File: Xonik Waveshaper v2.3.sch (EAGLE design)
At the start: 77 parts, among them IC1 TL074JT, IC2 TL074JT, IC3 TL074JT, IC4 TL072JT, IC5 4013T, IC6 LM311D, T1 2n3904

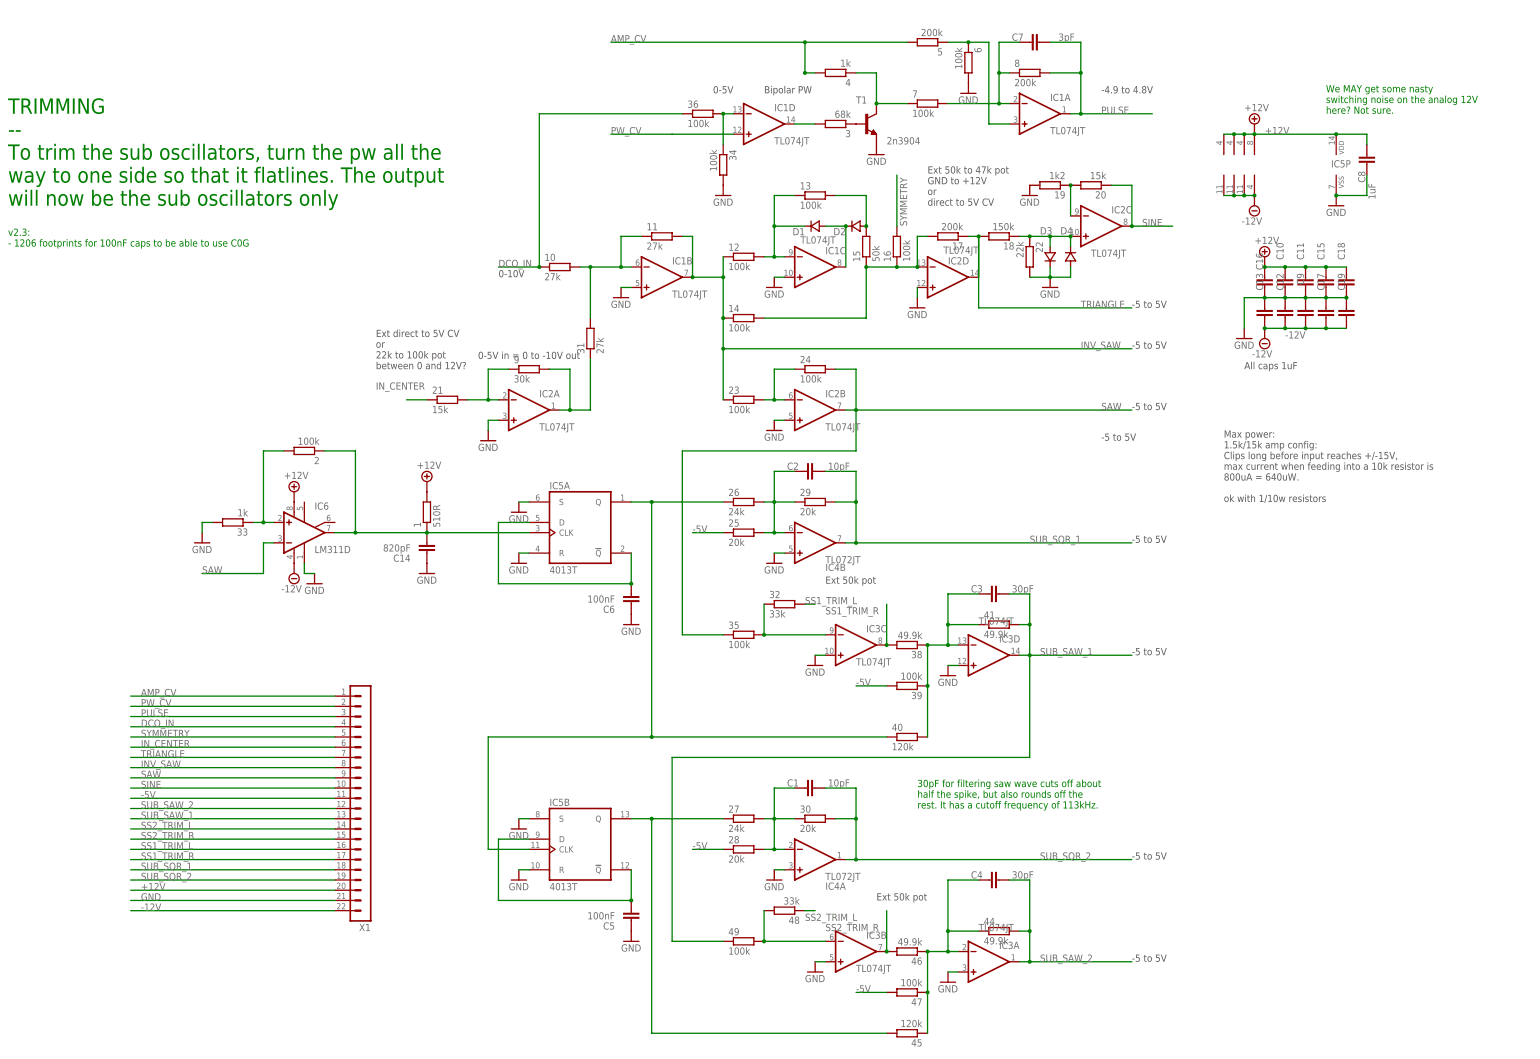
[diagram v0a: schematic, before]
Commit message: Replaced LM311 with op amp comparator
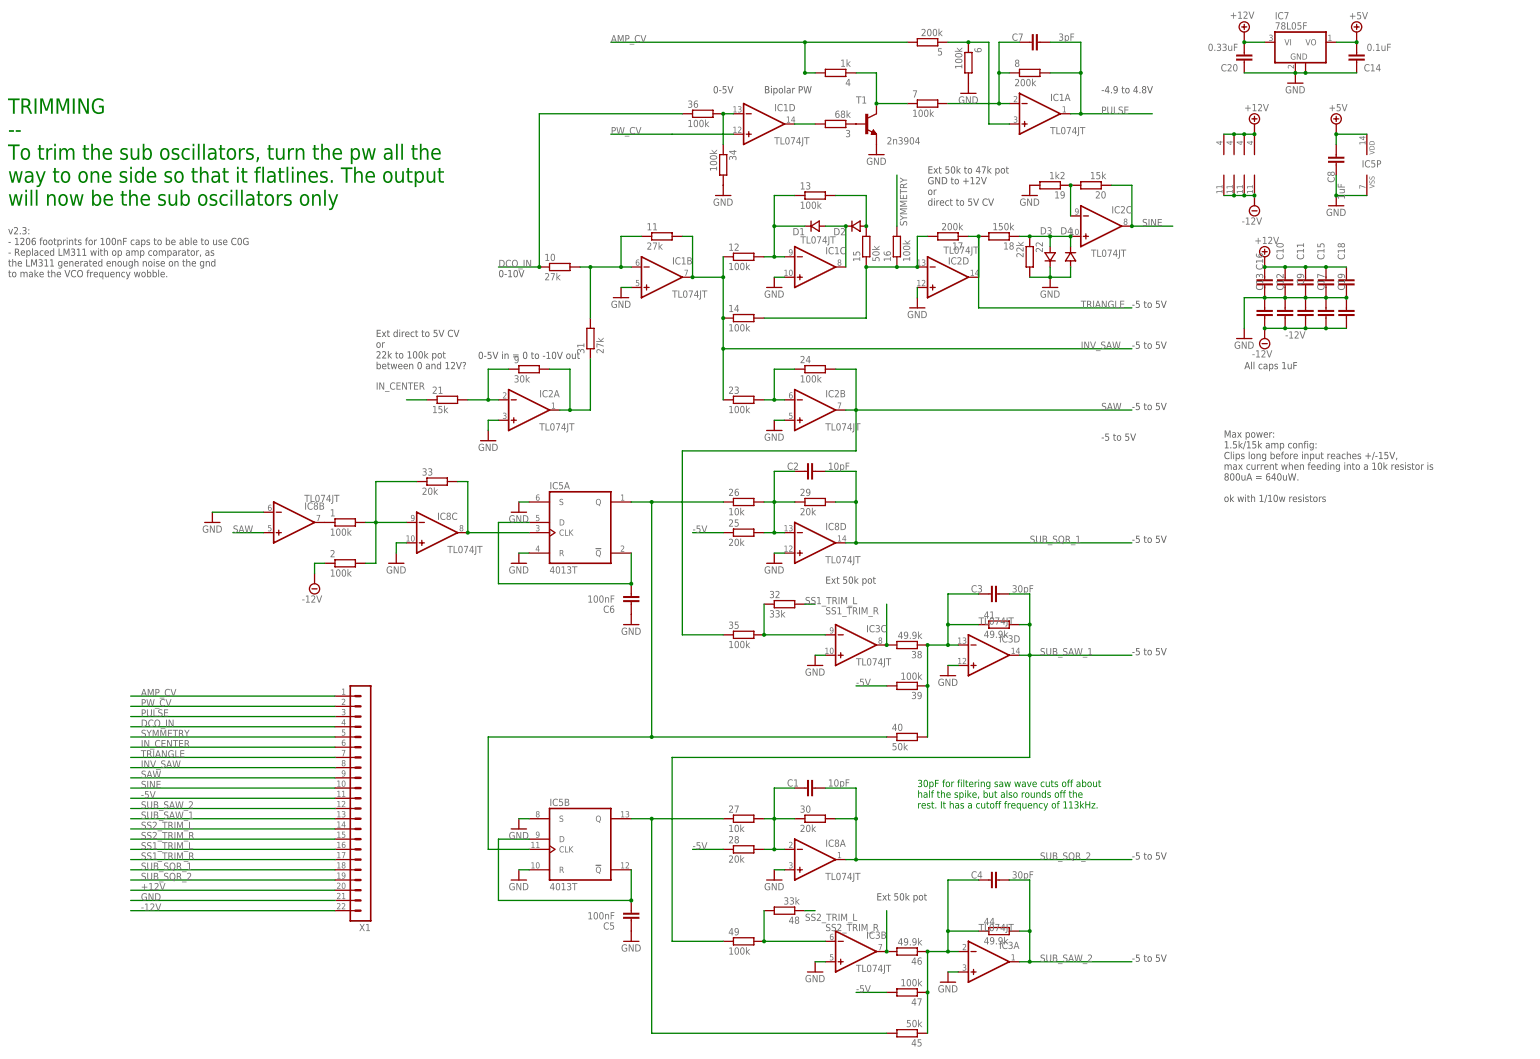
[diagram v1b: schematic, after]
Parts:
- removed IC4: TL072JT, joakim:TL072JT
- removed IC6: LM311D, joakim:LM311D
- added C20: 0.33uF, resistor:C-EUC0603
- added IC7: 78L05F, linear:78L05F
- added IC8: TL074JT, joakim:TL074JT
- 1: value 510R -> 100k
- 26, 27: value 24k -> 10k
- 33: value 1k -> 20k
- 40, 45: value 120k -> 50k
- C14: value 820pF -> 0.1uF; device joakim:C-EU-J0603 -> resistor:C-EUC0603
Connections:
- removed net N$25: 2.2, 33.1, IC6.+IN
- removed net SQR: 1.1, 2.1, C14.2, IC5A.CLK, IC6.OUT
- new net +5V: C14.2, C8.2, IC5P.VDD, IC7.VO
- new net N$17: 33.2, IC5A.CLK, IC8C.OUT
- new net N$7: 1.1, IC8B.OUT
- new net N$9: 1.2, 2.2, 33.1, IC8C.-IN
- net +12V: now also C20.2, IC7.VI, IC8P.V+; no longer 1.2, C8.2, IC4P.V+, IC5P.VDD, IC6.V+
- net -12V: now also 2.1, IC8P.V-; no longer IC4P.V-, IC6.V-
- net GND: now also C20.1, IC7.GND, IC7.GND@1, IC8A.+IN, IC8B.-IN, IC8C.+IN, IC8D.+IN; no longer 33.2, IC4A.+IN, IC4B.+IN, IC6.GND
- net N$19: now also IC8D.-IN; no longer IC4B.-IN
- net N$22: now also IC8A.-IN; no longer IC4A.-IN
- net SAW: now also IC8B.+IN; no longer IC6.-IN
- net SUB_SQR_1: now also IC8D.OUT; no longer IC4B.OUT
- net SUB_SQR_2: now also IC8A.OUT; no longer IC4A.OUT
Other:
- note added: "v2.3: - 1206 footprints for 100nF caps to be able to use C0G - Replaced LM311 with op amp comparator, as the LM311 generated enough noise on the gnd to make the VCO frequency wobble."
- note removed: "We MAY get some nasty switching noise on the analog 12V here? Not sure."
- note removed: "v2.3: - 1206 footprints for 100nF caps to be able to use C0G"
- moved on the sheet: 1, 2, 33, C14, C8, IC5P

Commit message: Routed new version of comparator
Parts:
- removed C14: 0.1uF, resistor:C-EUC0603
- removed C18, C19: 1uF, joakim:C-EU-J0402
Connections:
- net +12V: no longer C18.2
- net +5V: no longer C14.2
- net -12V: no longer C19.1
- net GND: no longer C14.1, C18.1, C19.2
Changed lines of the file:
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@@
 <part name="C15" library="joakim" deviceset="C-EU-J" device="0402" value="1uF"/>
 <part name="C17" library="joakim" deviceset="C-EU-J" device="0402" value="1uF"/>
-<part name="C18" library="joakim" deviceset="C-EU-J" device="0402" value="1uF"/>
-<part name="C19" library="joakim" deviceset="C-EU-J" device="0402" value="1uF"/>
 <part name="34" library="rcl" library_urn="urn:adsk.eagle:library:334" deviceset="R-EU_" device="R0402" package3d_urn="urn:adsk.eagle:package:23547/3" value="100k"/>
 <part name="36" library="rcl" library_urn="urn:adsk.eagle:library:334" deviceset="R-EU_" device="R0402" package3d_urn="urn:adsk.eagle:package:23547/3" value="100k"/>
@@
 <part name="IC7" library="linear" library_urn="urn:adsk.eagle:library:262" deviceset="78L*" device="F" package3d_urn="urn:adsk.eagle:package:16478/2" technology="05"/>
 <part name="SUPPLY5" library="supply2" library_urn="urn:adsk.eagle:library:372" deviceset="+5V" device=""/>
-<part name="C14" library="resistor" deviceset="C-EU" device="C0603" value="0.1uF"/>
 <part name="C20" library="resistor" deviceset="C-EU" device="C0603" value="0.33uF"/>
 <part name="P+3" library="supply2" library_urn="urn:adsk.eagle:library:372" deviceset="+12V" device=""/>
@@
 <attribute name="NAME" x="147.701" y="46.736" size="1.778" layer="95" rot="R270"/>
 </instance>
-<instance part="C18" gate="G$1" x="154.94" y="43.18" smashed="yes" rot="R180">
-<attribute name="NAME" x="152.781" y="54.356" size="1.778" layer="95" rot="R270"/>
-</instance>
-<instance part="C19" gate="G$1" x="154.94" y="35.56" smashed="yes" rot="R180">
-<attribute name="NAME" x="152.781" y="46.736" size="1.778" layer="95" rot="R270"/>
-</instance>
 <instance part="IC1" gate="A" x="78.74" y="86.36" smashed="yes">
 <attribute name="NAME" x="81.28" y="89.535" size="1.778" layer="95"/>
@@
 <instance part="SUPPLY5" gate="+5V" x="157.48" y="106.68" smashed="yes">
 <attribute name="VALUE" x="155.575" y="109.855" size="1.778" layer="96"/>
-</instance>
-<instance part="C14" gate="G$1" x="157.48" y="99.06" smashed="yes" rot="R180">
-<attribute name="NAME" x="163.576" y="98.679" size="1.778" layer="95" rot="R180"/>
-<attribute name="VALUE" x="166.116" y="103.759" size="1.778" layer="96" rot="R180"/>
 </instance>
 <instance part="C20" gate="G$1" x="129.54" y="99.06" smashed="yes" rot="R180">
@@
 <wire x1="144.78" y1="40.64" x2="149.86" y2="40.64" width="0.1524" layer="91"/>
 <junction x="149.86" y="40.64"/>
-<pinref part="C18" gate="G$1" pin="1"/>
-<pinref part="C19" gate="G$1" pin="2"/>
-<wire x1="149.86" y1="40.64" x2="154.94" y2="40.64" width="0.1524" layer="91"/>
-<junction x="154.94" y="40.64"/>
 </segment>
 <segment>
@@
 <pinref part="IC7" gate="G$1" pin="GND@1"/>
 <wire x1="144.78" y1="96.52" x2="142.24" y2="96.52" width="0.1524" layer="91"/>
-<junction x="144.78" y="96.52"/>
-<pinref part="C14" gate="G$1" pin="1"/>
-<wire x1="157.48" y1="96.52" x2="144.78" y2="96.52" width="0.1524" layer="91"/>
 <pinref part="GND14" gate="1" pin="GND"/>
 </segment>
@@
 <junction x="134.62" y="48.26"/>
 <pinref part="C15" gate="G$1" pin="2"/>
-<wire x1="149.86" y1="48.26" x2="154.94" y2="48.26" width="0.1524" layer="91"/>
-<junction x="149.86" y="48.26"/>
-<pinref part="C18" gate="G$1" pin="2"/>
 </segment>
 <segment>
@@
 <junction x="144.78" y="33.02"/>
 <pinref part="C17" gate="G$1" pin="1"/>
-<wire x1="149.86" y1="33.02" x2="154.94" y2="33.02" width="0.1524" layer="91"/>
-<junction x="149.86" y="33.02"/>
-<pinref part="C19" gate="G$1" pin="1"/>
 </segment>
 <segment>
@@
 <pinref part="SUPPLY5" gate="+5V" pin="+5V"/>
 <wire x1="152.4" y1="104.14" x2="157.48" y2="104.14" width="0.1524" layer="91"/>
-<pinref part="C14" gate="G$1" pin="2"/>
-<junction x="157.48" y="104.14"/>
-</segment>
-</net>
+</segment>
+</net>

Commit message: Improved cap footprint
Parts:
- C20: device resistor:C-EUC0603 -> joakim:C-EU-J0603
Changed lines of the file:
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@@
 <part name="IC7" library="linear" library_urn="urn:adsk.eagle:library:262" deviceset="78L*" device="F" package3d_urn="urn:adsk.eagle:package:16478/2" technology="05"/>
 <part name="SUPPLY5" library="supply2" library_urn="urn:adsk.eagle:library:372" deviceset="+5V" device=""/>
-<part name="C20" library="resistor" deviceset="C-EU" device="C0603" value="0.33uF"/>
+<part name="C20" library="joakim" deviceset="C-EU-J" device="0603" value="0.33uF"/>
 <part name="P+3" library="supply2" library_urn="urn:adsk.eagle:library:372" deviceset="+12V" device=""/>
 <part name="GND14" library="supply1" library_urn="urn:adsk.eagle:library:371" deviceset="GND" device=""/>

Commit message: Comment about testing
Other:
- note added: "Sub oscillator circuit tested on the 2nd of January 2025"
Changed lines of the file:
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@@
 the LM311 generated enough noise on the gnd
 to make the VCO frequency wobble.</text>
+<text x="-177.8" y="35.56" size="1.778" layer="91">Sub oscillator circuit
+tested on the 2nd of January 2025</text>
 </plain>
 <instances>

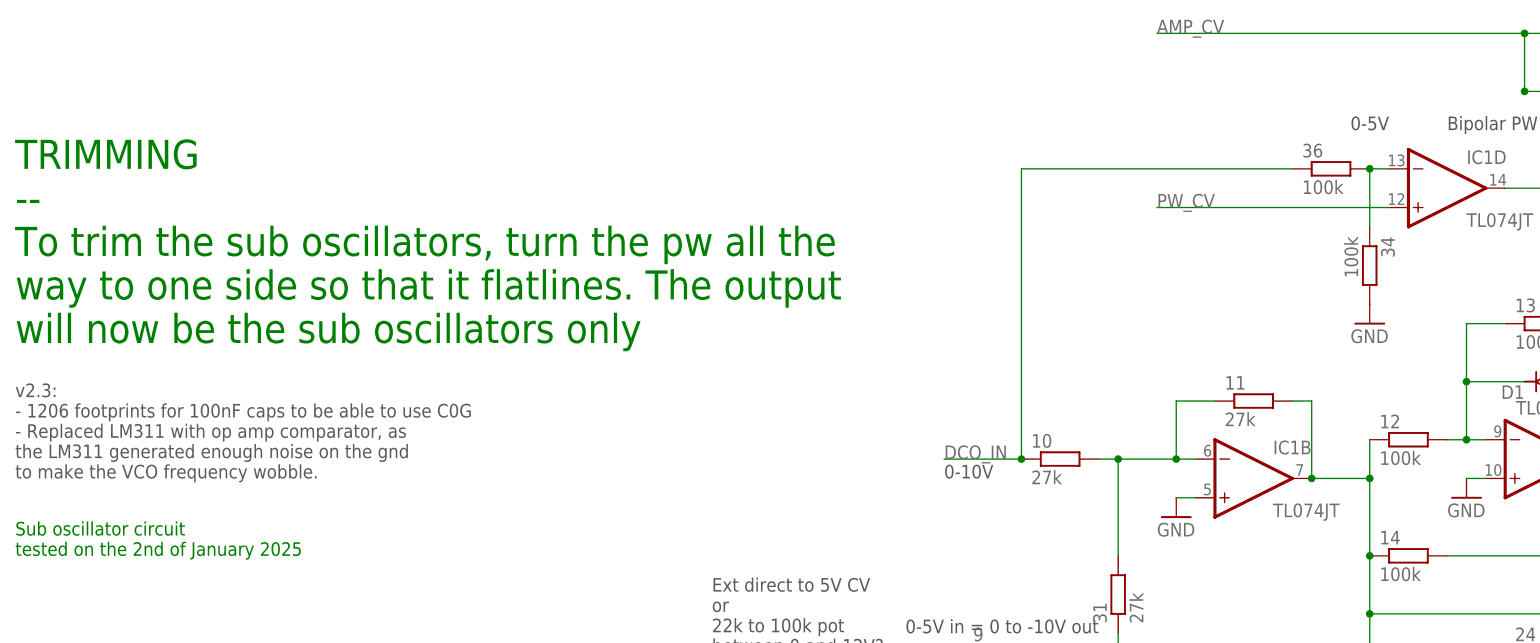
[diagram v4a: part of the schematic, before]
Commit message: Fixed polarity issue on square wave output
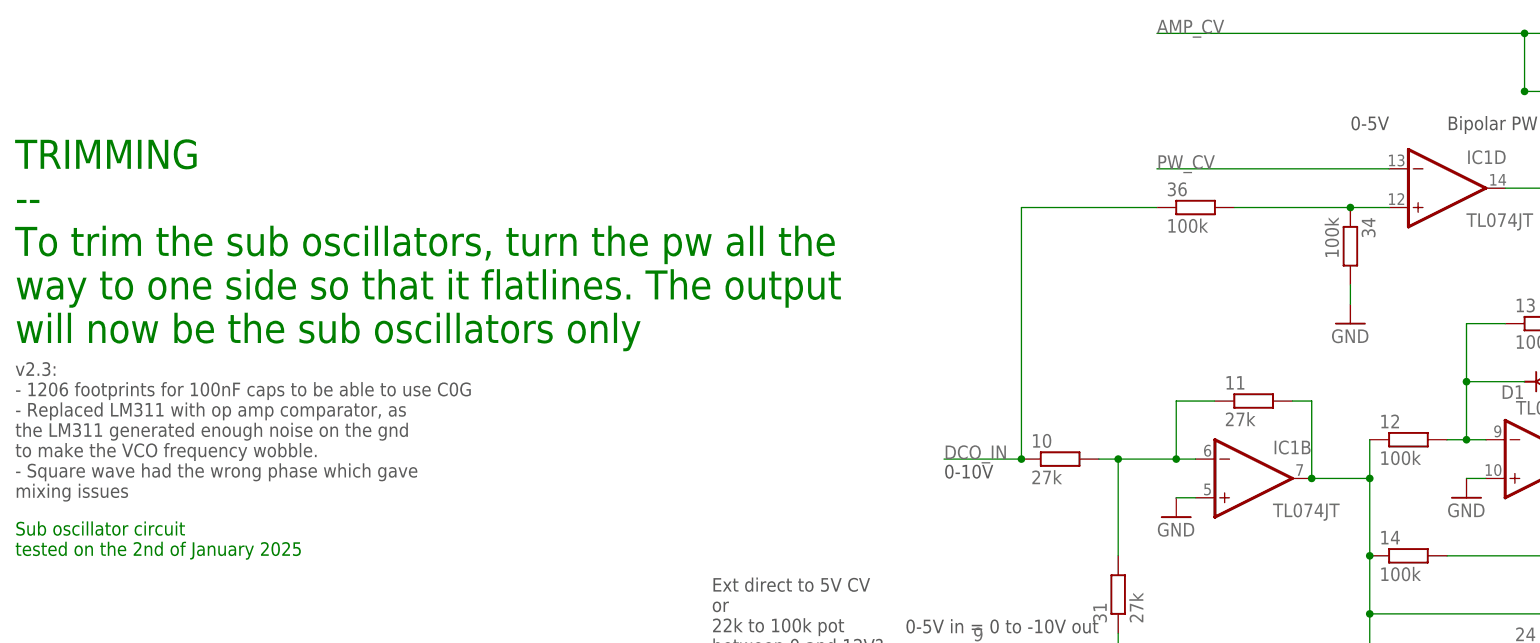
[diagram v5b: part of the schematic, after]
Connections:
- net N$8: now also IC1D.+IN; no longer IC1D.-IN
- net PW_CV: now also IC1D.-IN; no longer IC1D.+IN
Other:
- note added: "v2.3: - 1206 footprints for 100nF caps to be able to use C0G - Replaced LM311 with op amp comparator, as the LM311 generated enough noise on the gnd to make the VCO frequency wobble. - Square wave had the wrong phase which gave mixing issues"
- note removed: "v2.3: - 1206 footprints for 100nF caps to be able to use C0G - Replaced LM311 with op amp comparator, as the LM311 generated enough noise on the gnd to make the VCO frequency wobble."
- moved on the sheet: 34, 36
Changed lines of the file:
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@@
 way to one side so that it flatlines. The output
 will now be the sub oscillators only </text>
-<text x="-177.8" y="45.72" size="1.778" layer="97">v2.3:
+<text x="-177.8" y="43.18" size="1.778" layer="97">v2.3:
 - 1206 footprints for 100nF caps to be able to use C0G
 - Replaced LM311 with op amp comparator, as
 the LM311 generated enough noise on the gnd
-to make the VCO frequency wobble.</text>
+to make the VCO frequency wobble.
+- Square wave had the wrong phase which gave
+mixing issues</text>
 <text x="-177.8" y="35.56" size="1.778" layer="91">Sub oscillator circuit
 tested on the 2nd of January 2025</text>
@@
 <attribute name="VALUE" x="25.4" y="7.62" size="1.778" layer="96"/>
 </instance>
-<instance part="34" gate="G$1" x="0" y="73.66" smashed="yes" rot="R270">
-<attribute name="NAME" x="1.4986" y="77.47" size="1.778" layer="95" rot="R270"/>
-<attribute name="VALUE" x="-3.302" y="77.47" size="1.778" layer="96" rot="R270"/>
-</instance>
-<instance part="36" gate="G$1" x="-5.08" y="86.36" smashed="yes">
-<attribute name="NAME" x="-8.89" y="87.8586" size="1.778" layer="95"/>
-<attribute name="VALUE" x="-8.89" y="83.058" size="1.778" layer="96"/>
-</instance>
-<instance part="GND25" gate="1" x="0" y="66.04" smashed="yes">
-<attribute name="VALUE" x="-2.54" y="63.5" size="1.778" layer="96"/>
+<instance part="34" gate="G$1" x="-2.54" y="76.2" smashed="yes" rot="R270">
+<attribute name="NAME" x="-1.0414" y="80.01" size="1.778" layer="95" rot="R270"/>
+<attribute name="VALUE" x="-5.842" y="80.01" size="1.778" layer="96" rot="R270"/>
+</instance>
+<instance part="36" gate="G$1" x="-22.86" y="81.28" smashed="yes">
+<attribute name="NAME" x="-26.67" y="82.7786" size="1.778" layer="95"/>
+<attribute name="VALUE" x="-26.67" y="77.978" size="1.778" layer="96"/>
+</instance>
+<instance part="GND25" gate="1" x="-2.54" y="66.04" smashed="yes">
+<attribute name="VALUE" x="-5.08" y="63.5" size="1.778" layer="96"/>
 </instance>
 <instance part="X1" gate="G$1" x="-88.9" y="-81.28" smashed="yes" rot="R180">
@@
 <pinref part="34" gate="G$1" pin="2"/>
 <pinref part="GND25" gate="1" pin="GND"/>
+<wire x1="-2.54" y1="71.12" x2="-2.54" y2="68.58" width="0.1524" layer="91"/>
 </segment>
 <segment>
@@
 <wire x1="-45.72" y1="48.26" x2="-55.88" y2="48.26" width="0.1524" layer="91"/>
 <label x="-55.88" y="48.26" size="1.778" layer="95"/>
-<wire x1="-45.72" y1="48.26" x2="-45.72" y2="86.36" width="0.1524" layer="91"/>
+<wire x1="-45.72" y1="48.26" x2="-45.72" y2="81.28" width="0.1524" layer="91"/>
 <junction x="-45.72" y="48.26"/>
 <pinref part="36" gate="G$1" pin="1"/>
-<wire x1="-45.72" y1="86.36" x2="-10.16" y2="86.36" width="0.1524" layer="91"/>
+<wire x1="-45.72" y1="81.28" x2="-27.94" y2="81.28" width="0.1524" layer="91"/>
 </segment>
 <segment>
@@
 <net name="PW_CV" class="0">
 <segment>
-<wire x1="-27.94" y1="81.28" x2="-12.7" y2="81.28" width="0.1524" layer="91"/>
-<wire x1="-12.7" y1="81.28" x2="2.54" y2="81.28" width="0.1524" layer="91"/>
-<pinref part="IC1" gate="D" pin="+IN"/>
-<label x="-27.94" y="81.28" size="1.778" layer="95"/>
+<wire x1="-27.94" y1="86.36" x2="2.54" y2="86.36" width="0.1524" layer="91"/>
+<label x="-27.94" y="86.36" size="1.778" layer="95"/>
+<pinref part="IC1" gate="D" pin="-IN"/>
 </segment>
 <segment>
@@
 <net name="N$8" class="0">
 <segment>
-<pinref part="IC1" gate="D" pin="-IN"/>
-<wire x1="2.54" y1="86.36" x2="0" y2="86.36" width="0.1524" layer="91"/>
 <pinref part="36" gate="G$1" pin="2"/>
-<junction x="0" y="86.36"/>
 <pinref part="34" gate="G$1" pin="1"/>
-<wire x1="0" y1="78.74" x2="0" y2="86.36" width="0.1524" layer="91"/>
-</segment>
-</net>
+<wire x1="-2.54" y1="81.28" x2="-17.78" y2="81.28" width="0.1524" layer="91"/>
+<pinref part="IC1" gate="D" pin="+IN"/>
+<wire x1="-2.54" y1="81.28" x2="2.54" y2="81.28" width="0.1524" layer="91"/>
+<junction x="-2.54" y="81.28"/>
+</segment>
+</net>
